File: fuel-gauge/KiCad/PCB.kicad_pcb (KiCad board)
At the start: 2 copper layers, 100.1 x 70 mm, 39 parts, among them P1 CONN_01X04, P2 CONN_01X04, P3 CONN_01X04, Q1 BSS84, Q2 BSS138, Q3 2N7002, SW1 Switch_SPDT_x2, U1 AQV252G, U2 SN74LVC1G08DBVR, U3 TLV3691IDCKR, U4 bq34z100pw

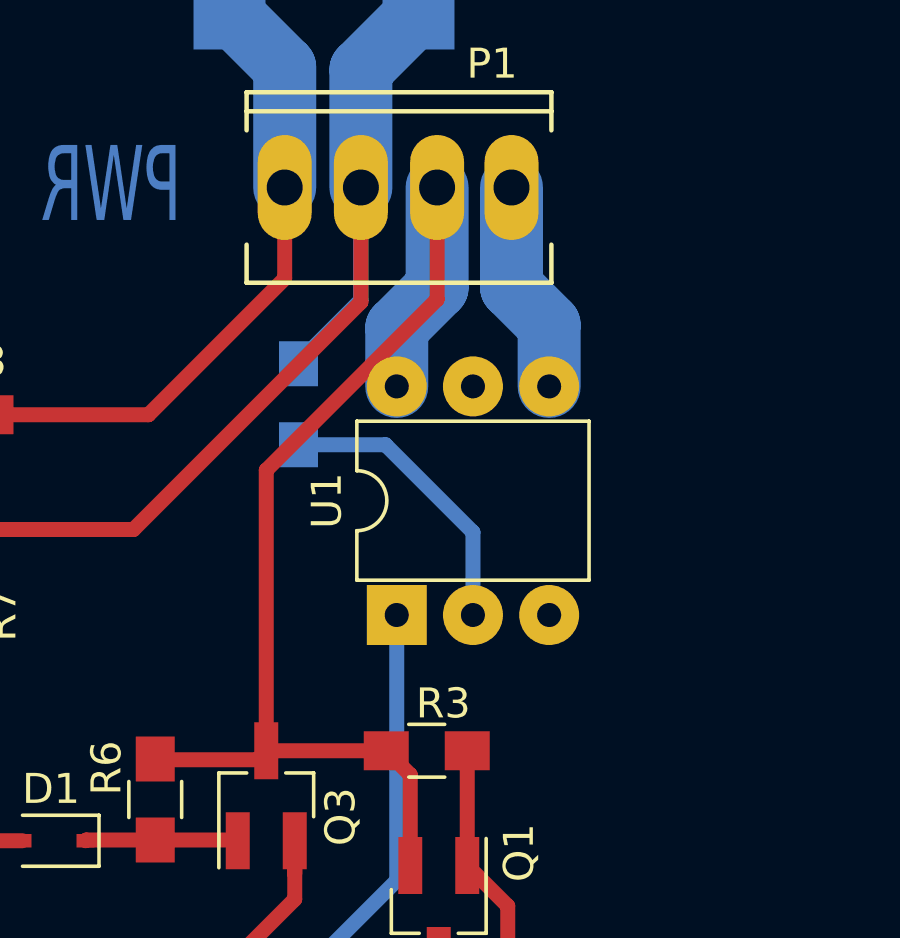
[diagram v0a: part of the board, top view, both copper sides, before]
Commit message: Modify the circuit in order to fit with the UGV v2.0 wiring
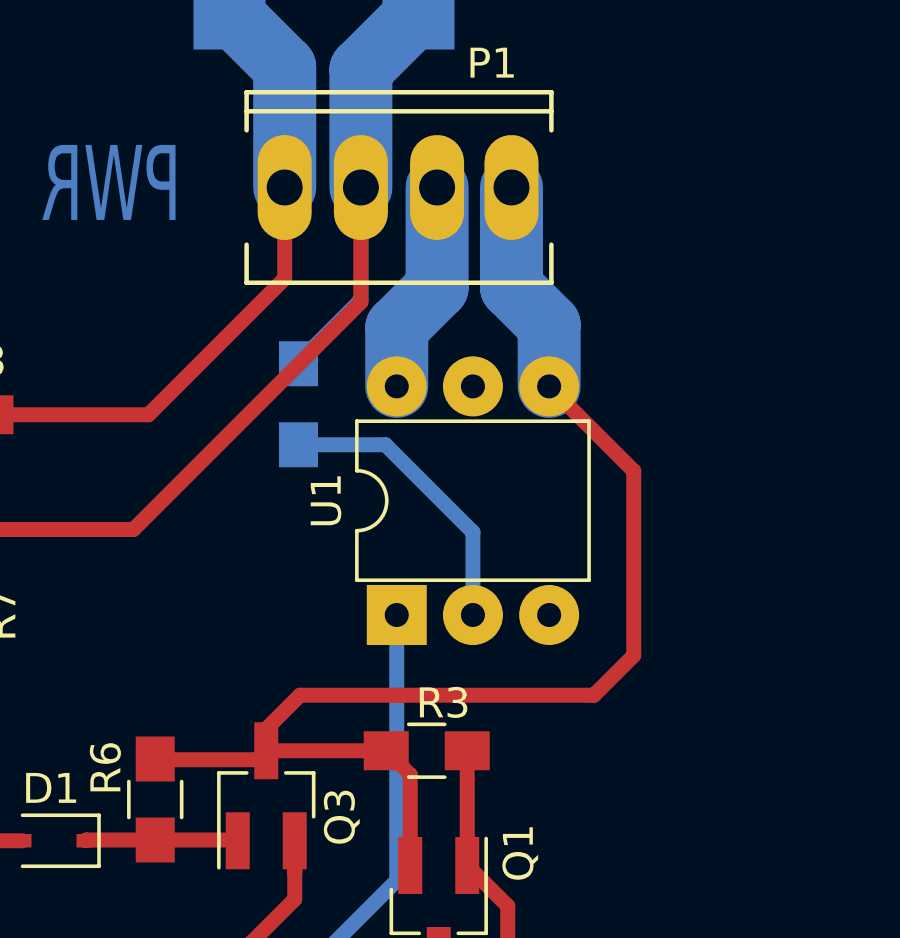
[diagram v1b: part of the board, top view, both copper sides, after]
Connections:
- Q1 pad 2: /BATT+ -> /PUSHBUTTON
- Q3 pad 3: /BATT+ -> /PUSHBUTTON
- R3 pad 1: /BATT+ -> /PUSHBUTTON
- R6 pad 1: /BATT+ -> /PUSHBUTTON
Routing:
- net /PUSHBUTTON: track 8.14 -> 44.3 mm
- net /BATT+: track 40.3 -> 7.19 mm
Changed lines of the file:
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@@
     (links 76)
     (no_connects 0)
-    (area 94.899999 49.899999 218.428572 144.700001)
+    (area 99.874999 59.899999 200.050001 130.050001)
     (thickness 1.6)
     (drawings 21)
-    (tracks 342)
+    (tracks 345)
     (zones 0)
     (modules 39)
@@
       (net 13 "Net-(Q1-Pad1)"))
     (pad 2 smd rect (at -1.5 0.95 270) (size 1.9 0.8) (layers F.Cu F.Paste F.Mask)
-      (net 9 /BATT+))
+      (net 21 /PUSHBUTTON))
     (pad 3 smd rect (at 1.5 0 270) (size 1.9 0.8) (layers F.Cu F.Paste F.Mask)
       (net 14 "Net-(Q1-Pad3)"))
@@
       (net 2 REG_IN))
     (pad 3 smd rect (at 1.5 0 90) (size 1.9 0.8) (layers F.Cu F.Paste F.Mask)
-      (net 9 /BATT+))
+      (net 21 /PUSHBUTTON))
     (model ../../../../../../DATOS/UNIVERSIDAD/TFG/PCB/packages3D-master/packages3D-master/TO_SOT_Packages_SMD.3dshapes/SOT-23.wrl
       (at (xyz 0 0 0))
@@
     (fp_line (start 2.35 0.9) (end -2.35 0.9) (layer F.CrtYd) (width 0.05))
     (pad 1 smd rect (at -1.35 0) (size 1.5 1.3) (layers F.Cu F.Paste F.Mask)
-      (net 9 /BATT+))
+      (net 21 /PUSHBUTTON))
     (pad 2 smd rect (at 1.35 0) (size 1.5 1.3) (layers F.Cu F.Paste F.Mask)
       (net 13 "Net-(Q1-Pad1)"))
@@
     (fp_line (start 2.35 0.9) (end -2.35 0.9) (layer F.CrtYd) (width 0.05))
     (pad 1 smd rect (at -1.35 0 270) (size 1.5 1.3) (layers F.Cu F.Paste F.Mask)
-      (net 9 /BATT+))
+      (net 21 /PUSHBUTTON))
     (pad 2 smd rect (at 1.35 0 270) (size 1.5 1.3) (layers F.Cu F.Paste F.Mask)
       (net 6 "Net-(D1-Pad1)"))
@@
   (segment (start 141.375 89.05) (end 143.05 89.05) (width 0.5) (layer F.Cu) (net 8))
   (segment (start 143.05 89.05) (end 144.45 90.45) (width 0.5) (layer F.Cu) (net 8))
-  (segment (start 183.52 76.45) (end 183.52 80.18) (width 0.5) (layer F.Cu) (net 9))
-  (segment (start 177.825 85.875) (end 177.825 95.225) (width 0.5) (layer F.Cu) (net 9))
-  (segment (start 183.52 80.18) (end 177.825 85.875) (width 0.5) (layer F.Cu) (net 9))
   (segment (start 182.175 83.08) (end 182.175 81.125) (width 2.1) (layer B.Cu) (net 9))
   (segment (start 183.52 79.78) (end 183.52 76.45) (width 2.1) (layer B.Cu) (net 9))
   (segment (start 182.175 81.125) (end 183.52 79.78) (width 2.1) (layer B.Cu) (net 9))
-  (segment (start 181.825 95.225) (end 181.825 95.125) (width 0.5) (layer F.Cu) (net 9))
-  (segment (start 181.825 95.225) (end 177.825 95.225) (width 0.5) (layer F.Cu) (net 9))
-  (segment (start 182.625 99.05) (end 182.625 96.025) (width 0.5) (layer F.Cu) (net 9))
-  (segment (start 182.625 96.025) (end 181.825 95.225) (width 0.5) (layer F.Cu) (net 9))
-  (segment (start 174.2 95.525) (end 177.525 95.525) (width 0.5) (layer F.Cu) (net 9))
-  (segment (start 177.525 95.525) (end 177.825 95.225) (width 0.5) (layer F.Cu) (net 9))
   (segment (start 178.44 76.45) (end 178.44 72.44) (width 2.1) (layer B.Cu) (net 10))
   (segment (start 178.44 72.44) (end 176.6 70.6) (width 2.1) (layer B.Cu) (net 10))
@@
   (segment (start 134.15 111.175) (end 132.525 109.55) (width 0.5) (layer F.Cu) (net 20))
   (segment (start 139.9 111.2) (end 134.175 111.2) (width 0.5) (layer F.Cu) (net 20))
+  (segment (start 177.825 95.225) (end 177.825 94.5) (width 0.5) (layer F.Cu) (net 21))
+  (segment (start 177.825 94.5) (end 178.95 93.375) (width 0.5) (layer F.Cu) (net 21))
+  (segment (start 190.075 85.9) (end 187.255 83.08) (width 0.5) (layer F.Cu) (net 21))
+  (segment (start 190.075 92.05) (end 190.075 85.9) (width 0.5) (layer F.Cu) (net 21))
+  (segment (start 188.75 93.375) (end 190.075 92.05) (width 0.5) (layer F.Cu) (net 21))
+  (segment (start 178.95 93.375) (end 188.75 93.375) (width 0.5) (layer F.Cu) (net 21))
+  (segment (start 181.825 95.225) (end 181.825 95.125) (width 0.5) (layer F.Cu) (net 21))
+  (segment (start 181.825 95.225) (end 177.825 95.225) (width 0.5) (layer F.Cu) (net 21))
+  (segment (start 182.625 99.05) (end 182.625 96.025) (width 0.5) (layer F.Cu) (net 21))
+  (segment (start 182.625 96.025) (end 181.825 95.225) (width 0.5) (layer F.Cu) (net 21))
+  (segment (start 174.2 95.525) (end 177.525 95.525) (width 0.5) (layer F.Cu) (net 21))
+  (segment (start 177.525 95.525) (end 177.825 95.225) (width 0.5) (layer F.Cu) (net 21))
   (segment (start 187.255 83.08) (end 187.255 81.03) (width 2.1) (layer B.Cu) (net 21))
+  (segment (start 187.255 81.03) (end 186 79.775) (width 2.1) (layer B.Cu) (net 21))
   (segment (start 186 79.775) (end 186 76.45) (width 2.1) (layer B.Cu) (net 21))
-  (segment (start 187.255 81.03) (end 186 79.775) (width 2.1) (layer B.Cu) (net 21))
   (segment (start 186.7 77.15) (end 186 76.45) (width 0.5) (layer B.Cu) (net 21))
   (segment (start 147.125 101.925) (end 148.375 101.925) (width 0.5) (layer F.Cu) (net 22))

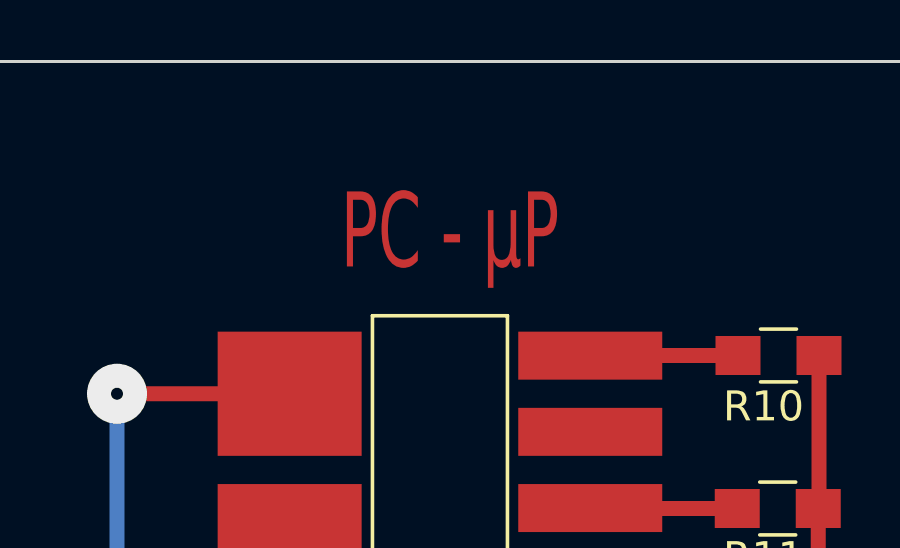
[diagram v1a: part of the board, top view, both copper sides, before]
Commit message: Correct SW1 positions and PWR connections
SW1 was well placed and wired but the text in copper layer that explains
the two posible positions was wrong.

PWR connector was wrong wired. Now all the circuit on the board is
supplied by the PUSHBUTTON terminal. In this way, when either the
Arduino, either the fuel gauge shut down the UGV, all the circuitry will
shut down.
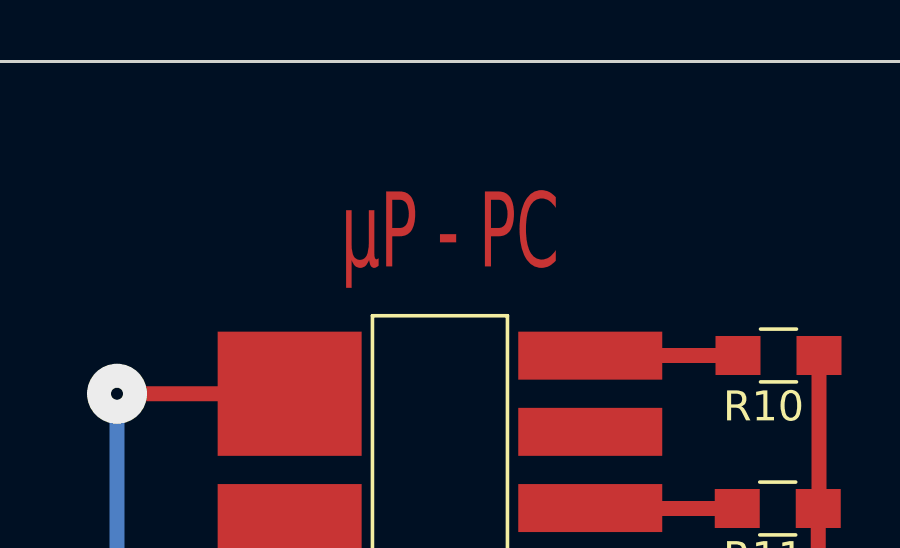
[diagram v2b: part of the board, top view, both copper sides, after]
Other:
- board text added: "µP - PC"
- board text removed: "PC - µP"
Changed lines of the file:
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@@
     (links 76)
     (no_connects 0)
-    (area 99.874999 59.899999 200.050001 130.050001)
+    (area 94.899999 49.899999 218.428572 144.700001)
     (thickness 1.6)
     (drawings 21)
@@
     (visible_elements 7FFFEE69)
     (pcbplotparams
-      (layerselection 0x00020_00000000)
+      (layerselection 0x00000_00000001)
       (usegerberextensions false)
       (excludeedgelayer false)
@@
     (effects (font (size 2.5 1.5) (thickness 0.375)) (justify mirror))
   )
-  (gr_text "PC - µP" (at 152.7 65.625) (layer F.Cu)
+  (gr_text "µP - PC" (at 152.7 65.625) (layer F.Cu)
     (effects (font (size 2.5 1.5) (thickness 0.375)))
   )

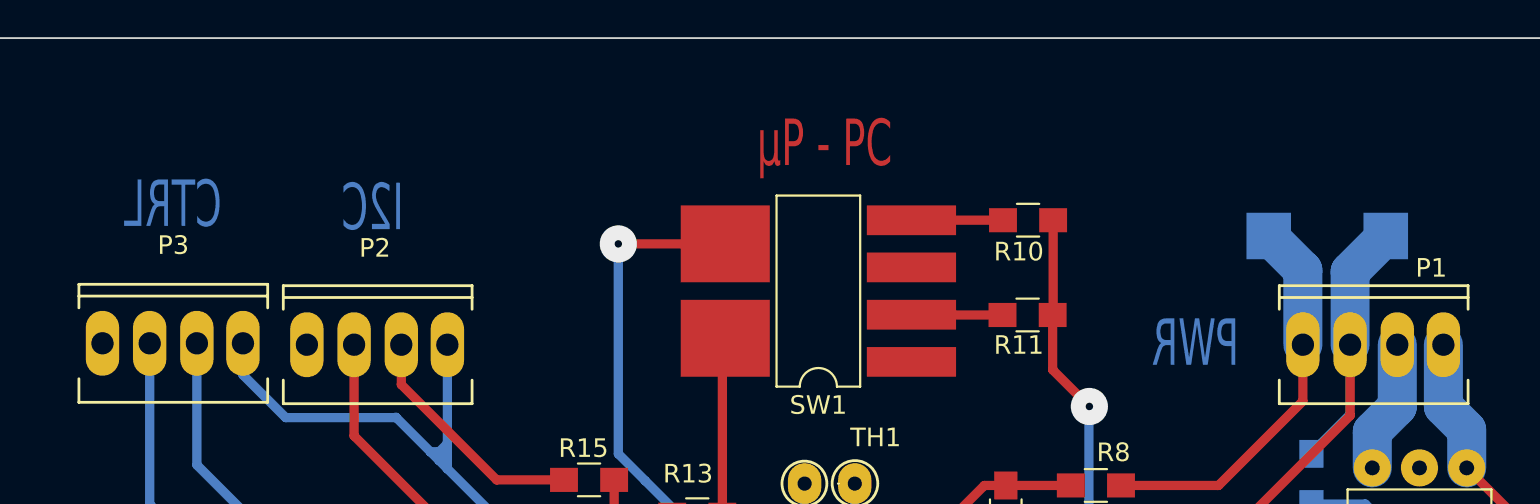
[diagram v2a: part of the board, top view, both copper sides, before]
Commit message: Add and relocate names in copper layers and update pdfs
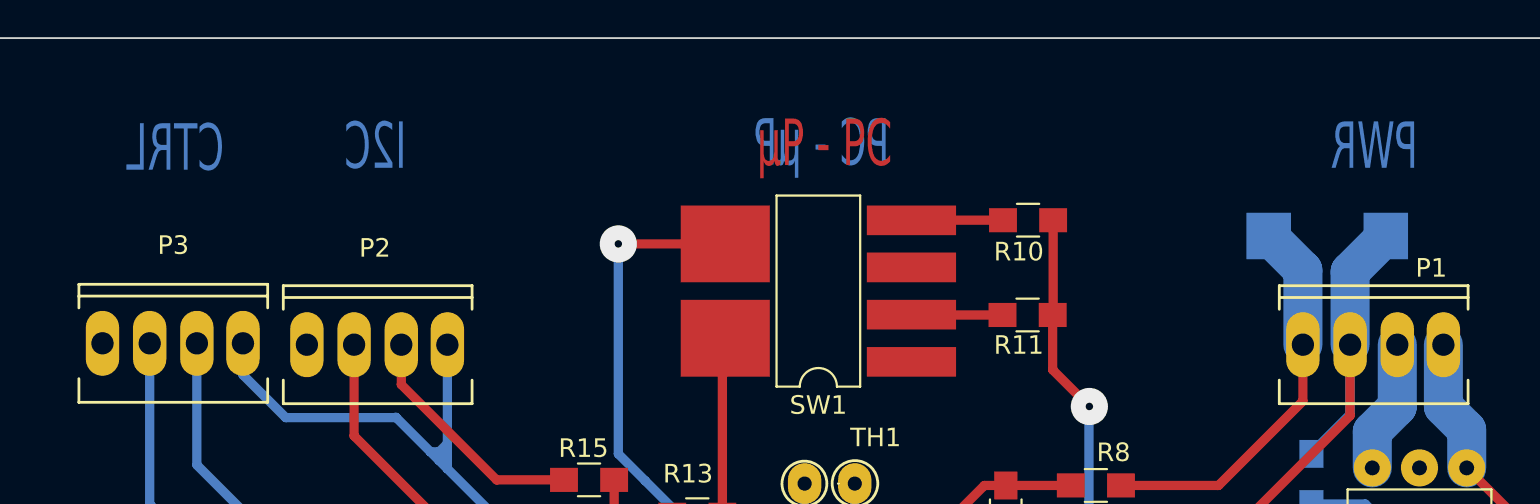
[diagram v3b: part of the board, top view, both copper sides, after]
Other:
- board text added: "PC - µP"
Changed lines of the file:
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@@
     (area 94.899999 49.899999 218.428572 144.700001)
     (thickness 1.6)
-    (drawings 21)
+    (drawings 22)
     (tracks 345)
     (zones 0)
@@
     )
   )
-  (gr_text PWR (at 172.65 76.375) (layer B.Cu)
+  (gr_text "PC - µP" (at 152.55 65.6) (layer B.Cu)
     (effects (font (size 2.5 1.5) (thickness 0.375)) (justify mirror))
   )
-  (gr_text CTRL (at 117.625 68.9) (layer B.Cu)
+  (gr_text PWR (at 182.275 65.775) (layer B.Cu)
     (effects (font (size 2.5 1.5) (thickness 0.375)) (justify mirror))
   )
-  (gr_text I2C (at 128.375 69.075) (layer B.Cu)
+  (gr_text CTRL (at 117.75 65.875) (layer B.Cu)
     (effects (font (size 2.5 1.5) (thickness 0.375)) (justify mirror))
   )
+  (gr_text I2C (at 128.525 65.775) (layer B.Cu)
+    (effects (font (size 2.5 1.5) (thickness 0.375)) (justify mirror))
+  )
